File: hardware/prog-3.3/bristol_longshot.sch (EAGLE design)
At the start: 2 parts

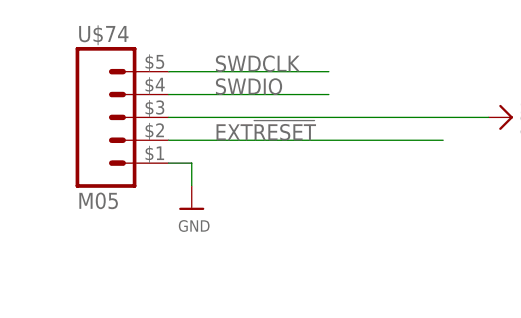
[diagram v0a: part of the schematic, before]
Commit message: Updated many parts lists, updated bard numbering, removed makefiles for inactive things
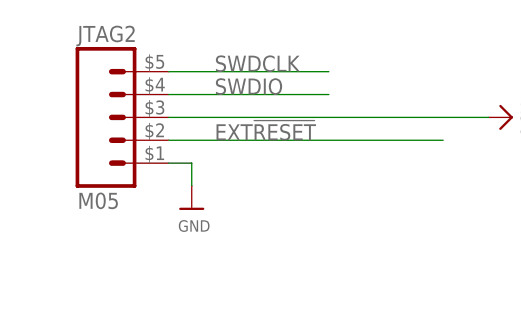
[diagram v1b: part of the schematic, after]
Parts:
- renumbered U$74 to JTAG2
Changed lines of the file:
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@@
 <part name="FRAME1" library="SparkFun" deviceset="FRAME-LETTER" device=""/>
 <part name="U$6" library="microbuilder_v3" deviceset="GND" device=""/>
-<part name="U$74" library="fbri" deviceset="M05" device=""/>
+<part name="JTAG2" library="fbri" deviceset="M05" device=""/>
 <part name="U$1" library="microbuilder_v3" deviceset="GND" device=""/>
 <part name="JTAG1" library="microbuilder_v3" deviceset="JTAG-CORTEXM3" device="SMT"/>
@@
 <instance part="FRAME1" gate="G$2" x="147.32" y="0"/>
 <instance part="U$6" gate="G$1" x="30.48" y="152.4"/>
-<instance part="U$74" gate="A" x="22.86" y="162.56"/>
+<instance part="JTAG2" gate="A" x="22.86" y="162.56"/>
 <instance part="U$1" gate="G$1" x="12.7" y="106.68"/>
 <instance part="JTAG1" gate="G$1" x="25.4" y="114.3"/>
@@
 <net name="GND" class="0">
 <segment>
-<pinref part="U$74" gate="A" pin="1"/>
+<pinref part="JTAG2" gate="A" pin="1"/>
 <wire x1="27.94" y1="157.48" x2="30.48" y2="157.48" width="0.1524" layer="91"/>
 <pinref part="U$6" gate="G$1" pin="GND"/>
@@
 <net name="SWDIO" class="0">
 <segment>
-<pinref part="U$74" gate="A" pin="4"/>
+<pinref part="JTAG2" gate="A" pin="4"/>
 <wire x1="27.94" y1="165.1" x2="45.72" y2="165.1" width="0.1524" layer="91"/>
 <label x="33.02" y="165.1" size="1.778" layer="95"/>
@@
 <net name="SWDCLK" class="0">
 <segment>
-<pinref part="U$74" gate="A" pin="5"/>
+<pinref part="JTAG2" gate="A" pin="5"/>
 <wire x1="27.94" y1="167.64" x2="45.72" y2="167.64" width="0.1524" layer="91"/>
 <label x="33.02" y="167.64" size="1.778" layer="95"/>
@@
 <net name="EXT!RESET" class="0">
 <segment>
-<pinref part="U$74" gate="A" pin="2"/>
+<pinref part="JTAG2" gate="A" pin="2"/>
 <wire x1="27.94" y1="160.02" x2="58.42" y2="160.02" width="0.1524" layer="91"/>
 <label x="33.02" y="160.02" size="1.778" layer="95"/>
@@
 </segment>
 <segment>
-<pinref part="U$74" gate="A" pin="3"/>
+<pinref part="JTAG2" gate="A" pin="3"/>
 <pinref part="U$3" gate="G$1" pin="3.3V"/>
 <wire x1="27.94" y1="162.56" x2="63.5" y2="162.56" width="0.1524" layer="91"/>
